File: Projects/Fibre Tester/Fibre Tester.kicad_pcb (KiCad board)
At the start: 2 copper layers, 36.5 x 48.2 mm, 8 parts, among them IC1 NE555, J1 JACK-PLUG1

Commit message: new file:   Libraries/My_Component_Footprints.pretty/Switch_Slide_3_way_pad_SMD.kicad_mod 	modified:   Projects/Fibre Tester/Fibre Tester-cache.lib 	renamed:    Projects/Fibre Tester/Fibre_Tester-eagle-import.dcm -> Projects/Fibre Tester/Fibre Tester-rescue.dcm 	new file:   Projects/Fibre Tester/Fibre Tester-rescue.lib 	new file:   Projects/Fibre Tester/Fibre Tester.bak 	modified:   Projects/Fibre Tester/Fibre Tester.kicad_pcb 	new file:   Projects/Fibre Tester/Fibre Tester.kicad_pcb-bak 	new file:   Projects/Fibre Tester/Fibre Tester.net 	modified:   Projects/Fibre Tester/Fibre Tester.pro 	modified:   Projects/Fibre Tester/Fibre Tester.sch 	deleted:    Projects/Fibre Tester/Fibre_Tester-eagle-import.lib 	new file:   Projects/Fibre Tester/fp-info-cache 	modified:   Projects/Fibre Tester/sym-lib-table
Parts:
- removed J1: JACK-PLUG1, Fibre Tester:SPC4078
- removed LED1: RED, Fibre Tester:LED5MM
- removed LED2: Green, Fibre Tester:LED5MM
- added BT1: Battery_Cell, Jumper:SolderJumper-2_P1.3mm_Open_Pad1.0x1.5mm, F.Cu at (131.8, 114.7)
- added D1: LED, LED_THT:LED_D5.0mm_Clear, F.Cu at (132.6, 80.5)
- added D2: LED, LED_THT:LED_D5.0mm_Clear, F.Cu at (139.6, 80.5)
- added S1: JS202011SCQN, digikey-footprints:Switch_Slide_JS202011SCQN, F.Cu at (151.1, 95.5)
- C1: value 10uF -> CP; footprint Fibre Tester:E5-8,5 -> Capacitor_THT:CP_Radial_D6.3mm_P2.50mm
- IC1: footprint Fibre Tester:DIL-08 -> Package_DIP:DIP-8_W7.62mm
- R1, R2, R3: footprint Fibre Tester:0207_10 -> Resistor_THT:R_Axial_DIN0309_L9.0mm_D3.2mm_P12.70mm_Horizontal
- moved R1 15.8 mm to (143.6, 87.6), turned to 180 degrees
- moved C1 14.7 mm to (142.6, 105.4), turned to 0 degrees
- moved IC1 12.5 mm to (131.2, 101.6)
- moved R2 11.6 mm to (130.9, 91.9)
- moved R3 6.23 mm to (143.6, 96.8), turned to 180 degrees
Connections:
- net +12V renamed VCC
- IC1 pad 2: Net-(C1-Pad+) -> Net-(C1-Pad1)
- IC1 pad 5: Net-(IC1-Pad5) -> (no net)
- IC1 pad 6: Net-(C1-Pad+) -> Net-(C1-Pad1)
- IC1 pad 7: Net-(IC1-Pad7) -> (no net)
- R3 pad 1: Net-(C1-Pad+) -> Net-(C1-Pad1)
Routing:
- net Net-(IC1-Pad3): track 13.2 -> 0.00 mm
- net Net-(D2-Pad2): track 12.8 -> 0.00 mm
- net Net-(D1-Pad1): track 9.20 -> 0.00 mm
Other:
- board outline removed
- rule pad_to_mask_clearance: 0.2 -> 0

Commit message: Updated Fibre Tester project
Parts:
- removed S1: JS202011SCQN, digikey-footprints:Switch_Slide_JS202011SCQN
- added H1: MountingHole, MountingHole:MountingHole_2.5mm, F.Cu at (112.3, 80.8)
- added H2: MountingHole, MountingHole:MountingHole_2.5mm, F.Cu at (146.4, 80.8)
- added H3: MountingHole, MountingHole:MountingHole_2.5mm, F.Cu at (112.4, 46.9)
- added H4: MountingHole, MountingHole:MountingHole_2.5mm, F.Cu at (146.4, 46.7)
- added REF**: KiCad-Logo2_5mm_SilkScreen, Symbol:KiCad-Logo2_5mm_SilkScreen, F.Cu at (112.9, 59.2)
- added SW1: SW_SPDT, My_Component_Footprints:SW_Slide_angle_SPDT_TB, F.Cu at (147.3, 59.5)
- BT1: footprint Jumper:SolderJumper-2_P1.3mm_Open_Pad1.0x1.5mm -> Connector_PinSocket_2.54mm:PinSocket_1x02_P2.54mm_Vertical
- R1: value 220 -> 47k; footprint Resistor_THT:R_Axial_DIN0309_L9.0mm_D3.2mm_P12.70mm_Horizontal -> Resistor_THT:R_Axial_DIN0207_L6.3mm_D2.5mm_P10.16mm_Horizontal
- R2: footprint Resistor_THT:R_Axial_DIN0309_L9.0mm_D3.2mm_P12.70mm_Horizontal -> Resistor_THT:R_Axial_DIN0207_L6.3mm_D2.5mm_P10.16mm_Horizontal
- R3: value 47k -> 220; footprint Resistor_THT:R_Axial_DIN0309_L9.0mm_D3.2mm_P12.70mm_Horizontal -> Resistor_THT:R_Axial_DIN0207_L6.3mm_D2.5mm_P10.16mm_Horizontal
- moved R3 52.2 mm to (130.2, 46.4), turned to 270 degrees
- moved D2 45.0 mm to (124.5, 38.1)
- moved C1 42.9 mm to (119.4, 69.3), turned to 180 degrees
- moved D1 42.4 mm to (132.1, 38.1)
- moved R1 36.9 mm to (123.8, 56.5), turned to 90 degrees
- moved IC1 35.8 mm to (127.0, 66.0)
- moved R2 35.8 mm to (135.9, 56.5), turned to 90 degrees
- moved BT1 35.0 mm to (125.0, 80.4), turned to 270 degrees
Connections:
- D1 pad 2: Net-(D1-Pad2) -> VCC
- R1 pad 1: Net-(IC1-Pad3) -> Net-(C1-Pad1)
- R1 pad 2: Net-(D1-Pad1) -> Net-(IC1-Pad3)
- R2 pad 1: Net-(D2-Pad2) -> Net-(IC1-Pad3)
- R2 pad 2: Net-(IC1-Pad3) -> Net-(D1-Pad1)
- R3 pad 1: Net-(C1-Pad1) -> Net-(D2-Pad2)
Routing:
- net GND: track 0.00 -> 59.6 mm
- net VCC: track 0.00 -> 52.0 mm
- net Net-(BT1-Pad1): track 0.00 -> 36.4 mm
- net Net-(IC1-Pad3): track 0.00 -> 34.4 mm
- net Net-(C1-Pad1): track 0.00 -> 30.0 mm
- net Net-(D1-Pad1): track 0.00 -> 9.83 mm
- net Net-(D2-Pad2): track 0.00 -> 9.57 mm
- added copper zone on B.Cu, net GND
- added copper zone on F.Cu, net GND
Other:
- board text added: "+ve"
- board text added: "Fibre Tester by Tony Bell V2.0"

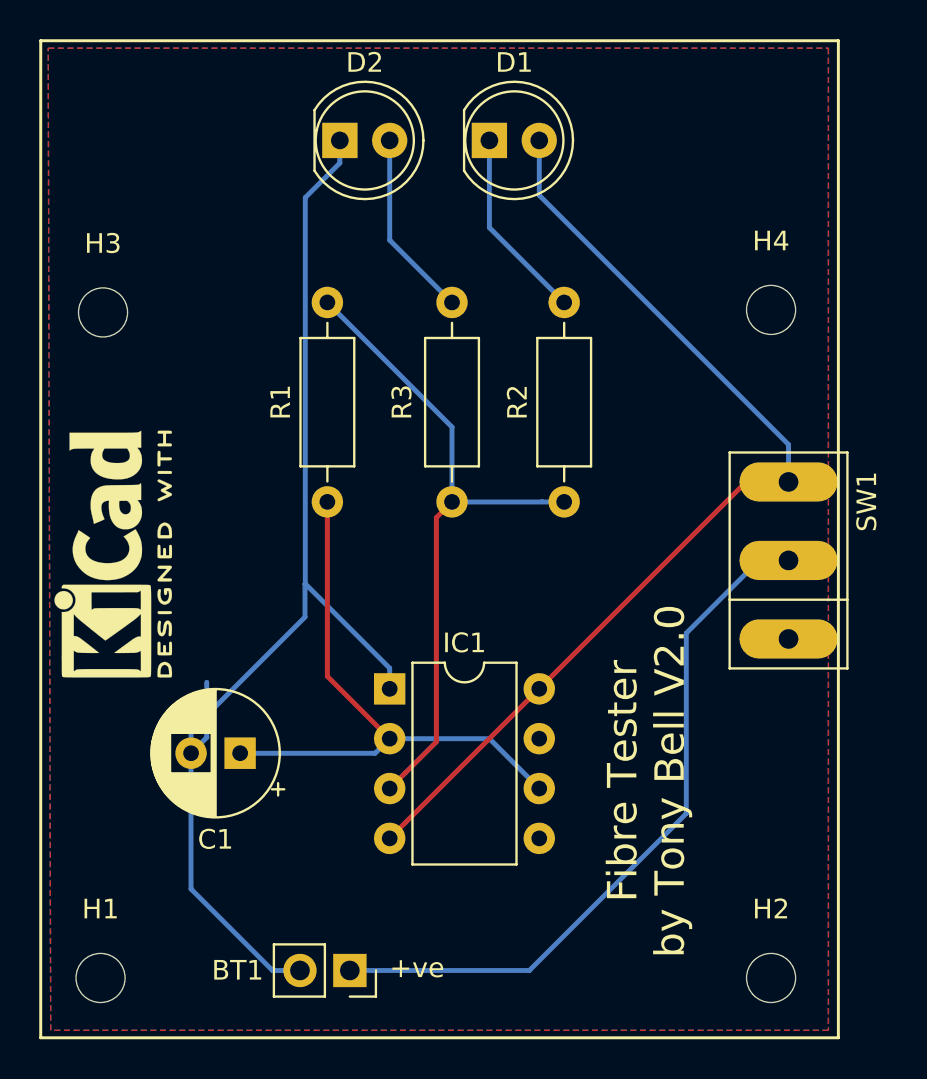
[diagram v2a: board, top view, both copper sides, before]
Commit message: Ammended overall PCB size to Fibre tester and ccreated Gerbers
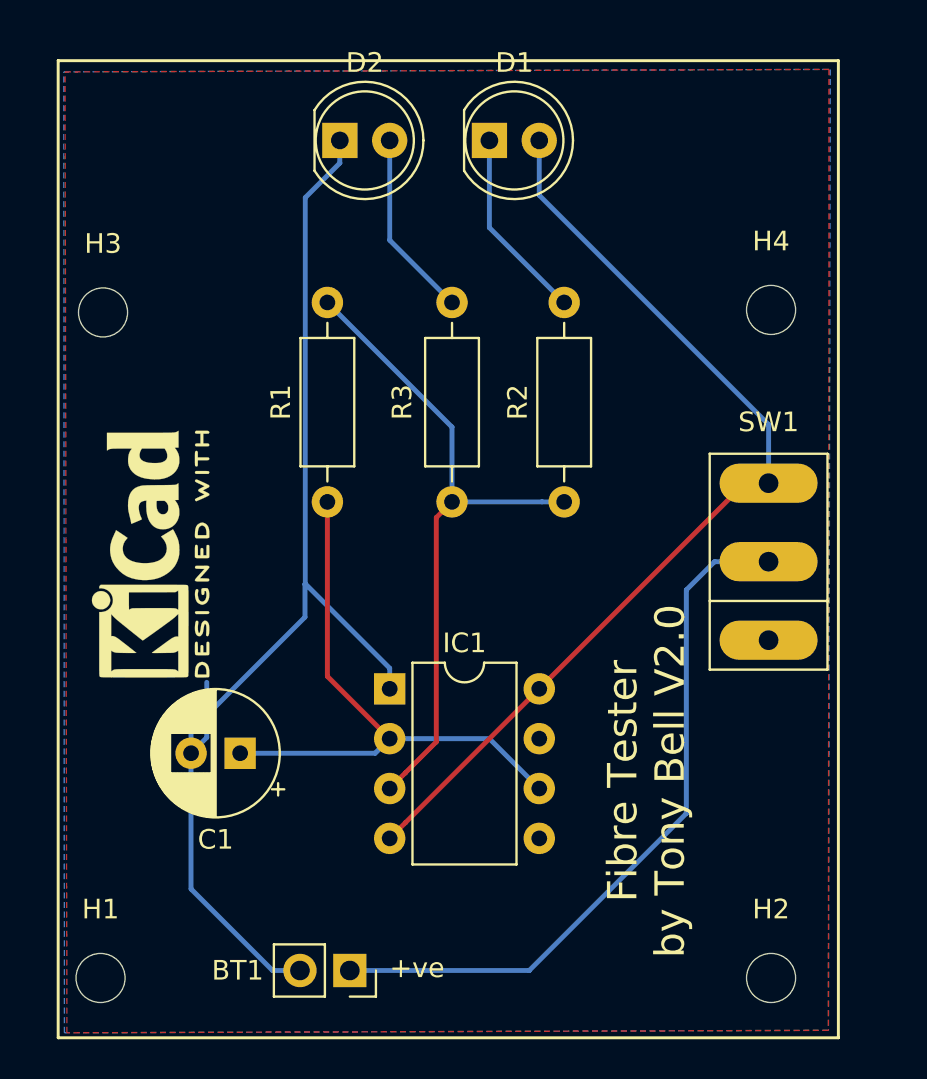
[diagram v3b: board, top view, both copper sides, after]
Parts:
- moved REF** 1.91 mm to (114.8, 59.2)
- moved SW1 1.02 mm to (146.3, 59.6)
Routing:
- net VCC: track 52.0 -> 54.2 mm
- net Net-(BT1-Pad1): track 36.4 -> 38.1 mm
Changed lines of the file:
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@@
     (thickness 1.6)
     (drawings 6)
-    (tracks 45)
+    (tracks 48)
     (zones 0)
     (modules 14)
@@
     (pad_to_mask_clearance 0)
     (aux_axis_origin 0 0)
-    (visible_elements FFFFFF7F)
+    (visible_elements 7FFFFFFF)
     (pcbplotparams
       (layerselection 0x010fc_ffffffff)
@@
       (outputformat 1)
       (mirror false)
-      (drillshape 1)
+      (drillshape 0)
       (scaleselection 1)
-      (outputdirectory ""))
+      (outputdirectory "Gerbers/"))
   )
   (net 0 "")
@@
   )
   (module Symbol:KiCad-Logo2_5mm_SilkScreen (layer F.Cu)
-    (at 112.903 59.182 90)
+    (at 114.808 59.182 90)
     (descr "KiCad Logo")
     (tags "Logo KiCad")
@@
   )
   (module My_Component_Footprints:SW_Slide_angle_SPDT_TB (layer F.Cu)
-    (at 147.32 59.5 90)
-    (fp_text reference SW1 (at 3 4 90) (layer F.SilkS)
+    (at 146.304 59.563 90)
+    (fp_text reference SW1 (at 7.112 0 180) (layer F.SilkS)
       (effects (font (size 1 1) (thickness 0.15)))
     )
@@
     (effects (font (size 1 1) (thickness 0.15)))
   )
-  (gr_line (start 109.22 33.02) (end 109.22 83.82) (layer F.SilkS) (width 0.15))
-  (gr_line (start 149.86 33.02) (end 109.22 33.02) (layer F.SilkS) (width 0.15))
-  (gr_line (start 149.86 83.82) (end 149.86 33.02) (layer F.SilkS) (width 0.15))
-  (gr_line (start 109.22 83.82) (end 149.86 83.82) (layer F.SilkS) (width 0.15))
+  (gr_line (start 110.109 34.036) (end 110.109 83.82) (layer F.SilkS) (width 0.15))
+  (gr_line (start 149.86 34.036) (end 110.109 34.036) (layer F.SilkS) (width 0.15))
+  (gr_line (start 149.86 83.82) (end 149.86 34.036) (layer F.SilkS) (width 0.15))
+  (gr_line (start 110.109 83.82) (end 149.86 83.82) (layer F.SilkS) (width 0.15))
   (segment (start 127 64.99) (end 127 66.04) (width 0.25) (layer B.Cu) (net 1))
   (segment (start 122.699999 60.689999) (end 127 64.99) (width 0.25) (layer B.Cu) (net 1))
@@
   (segment (start 122.682 60.707998) (end 122.699999 60.689999) (width 0.25) (layer B.Cu) (net 1))
   (segment (start 122.682 62.387631) (end 122.682 60.707998) (width 0.25) (layer B.Cu) (net 1))
-  (segment (start 124.968 80.391) (end 134.112 80.391) (width 0.25) (layer B.Cu) (net 2))
-  (segment (start 134.112 80.391) (end 142.113 72.39) (width 0.25) (layer B.Cu) (net 2))
   (segment (start 145.82 59.5) (end 147.32 59.5) (width 0.25) (layer B.Cu) (net 2))
-  (segment (start 142.113 63.207) (end 145.82 59.5) (width 0.25) (layer B.Cu) (net 2))
-  (segment (start 142.113 72.39) (end 142.113 63.207) (width 0.25) (layer B.Cu) (net 2))
+  (segment (start 134.112 80.391) (end 124.968 80.391) (width 0.25) (layer B.Cu) (net 2))
+  (segment (start 142.113 72.39) (end 134.112 80.391) (width 0.25) (layer B.Cu) (net 2))
+  (segment (start 142.113 61.004) (end 142.113 72.39) (width 0.25) (layer B.Cu) (net 2))
+  (segment (start 143.554 59.563) (end 142.113 61.004) (width 0.25) (layer B.Cu) (net 2))
+  (segment (start 146.304 59.563) (end 143.554 59.563) (width 0.25) (layer B.Cu) (net 2))
   (segment (start 126.258999 69.321001) (end 127 68.58) (width 0.25) (layer B.Cu) (net 3))
   (segment (start 119.38 69.321001) (end 126.258999 69.321001) (width 0.25) (layer B.Cu) (net 3))
@@
   (segment (start 145.82 55.5) (end 147.32 55.5) (width 0.25) (layer B.Cu) (net 5))
   (segment (start 134.62 38.1) (end 134.62 40.894) (width 0.25) (layer B.Cu) (net 5))
-  (segment (start 147.32 53.594) (end 147.32 55.5) (width 0.25) (layer B.Cu) (net 5))
-  (segment (start 134.62 40.894) (end 147.32 53.594) (width 0.25) (layer B.Cu) (net 5))
   (segment (start 127.799999 72.860001) (end 134.62 66.04) (width 0.25) (layer F.Cu) (net 5))
   (segment (start 127 73.66) (end 127.799999 72.860001) (width 0.25) (layer F.Cu) (net 5))
   (segment (start 145.16 55.5) (end 147.32 55.5) (width 0.25) (layer F.Cu) (net 5))
-  (segment (start 134.62 66.04) (end 145.16 55.5) (width 0.25) (layer F.Cu) (net 5))
+  (segment (start 145.097 55.563) (end 146.558 55.563) (width 0.25) (layer F.Cu) (net 5))
+  (segment (start 145.097 55.563) (end 146.304 55.563) (width 0.25) (layer F.Cu) (net 5))
+  (segment (start 134.62 66.04) (end 145.097 55.563) (width 0.25) (layer F.Cu) (net 5))
+  (segment (start 146.304 52.578) (end 146.304 55.563) (width 0.25) (layer B.Cu) (net 5))
+  (segment (start 134.62 40.894) (end 146.304 52.578) (width 0.25) (layer B.Cu) (net 5))
   (segment (start 127 43.18) (end 127 38.1) (width 0.25) (layer B.Cu) (net 6))
   (segment (start 130.175 46.355) (end 127 43.18) (width 0.25) (layer B.Cu) (net 6))
@@
     (polygon
       (pts
-        (xy 109.601 33.401) (xy 149.352 33.401) (xy 149.352 83.439) (xy 109.728 83.439)
+        (xy 110.39475 34.6075) (xy 149.44725 34.4805) (xy 149.352 83.439) (xy 110.4265 83.566)
       )
     )
@@
     (polygon
       (pts
-        (xy 109.601 33.401) (xy 149.352 33.401) (xy 149.352 83.439) (xy 109.728 83.439)
+        (xy 110.45825 34.6075) (xy 149.38375 34.4805) (xy 149.352 83.439) (xy 110.5535 83.566)
       )
     )
